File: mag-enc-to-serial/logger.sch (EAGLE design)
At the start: 28 parts, among them IC1 75176AD, IC2 REG1117, U1 MSP430G2352IPW14

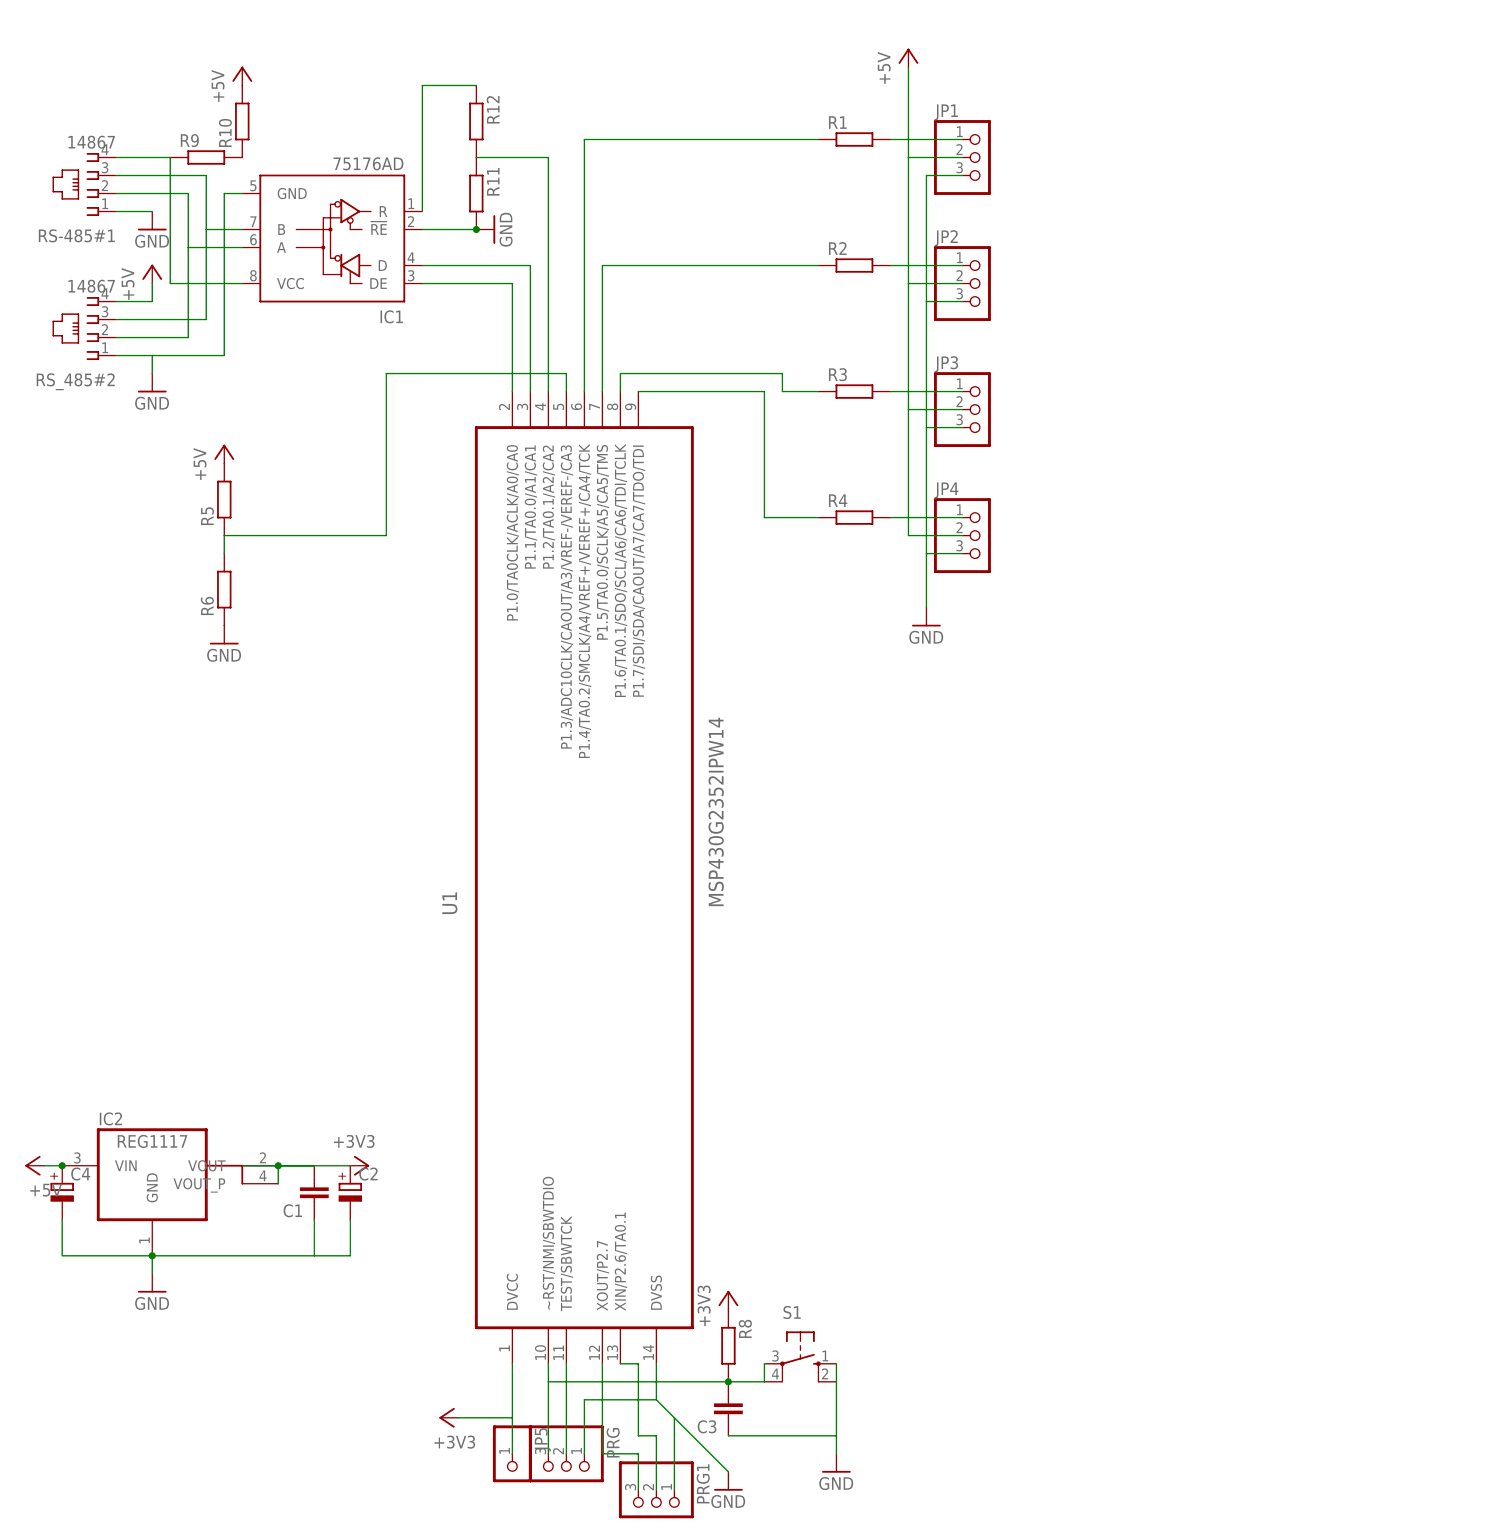
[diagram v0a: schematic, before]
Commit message: Magnetic encode with MSP430 board
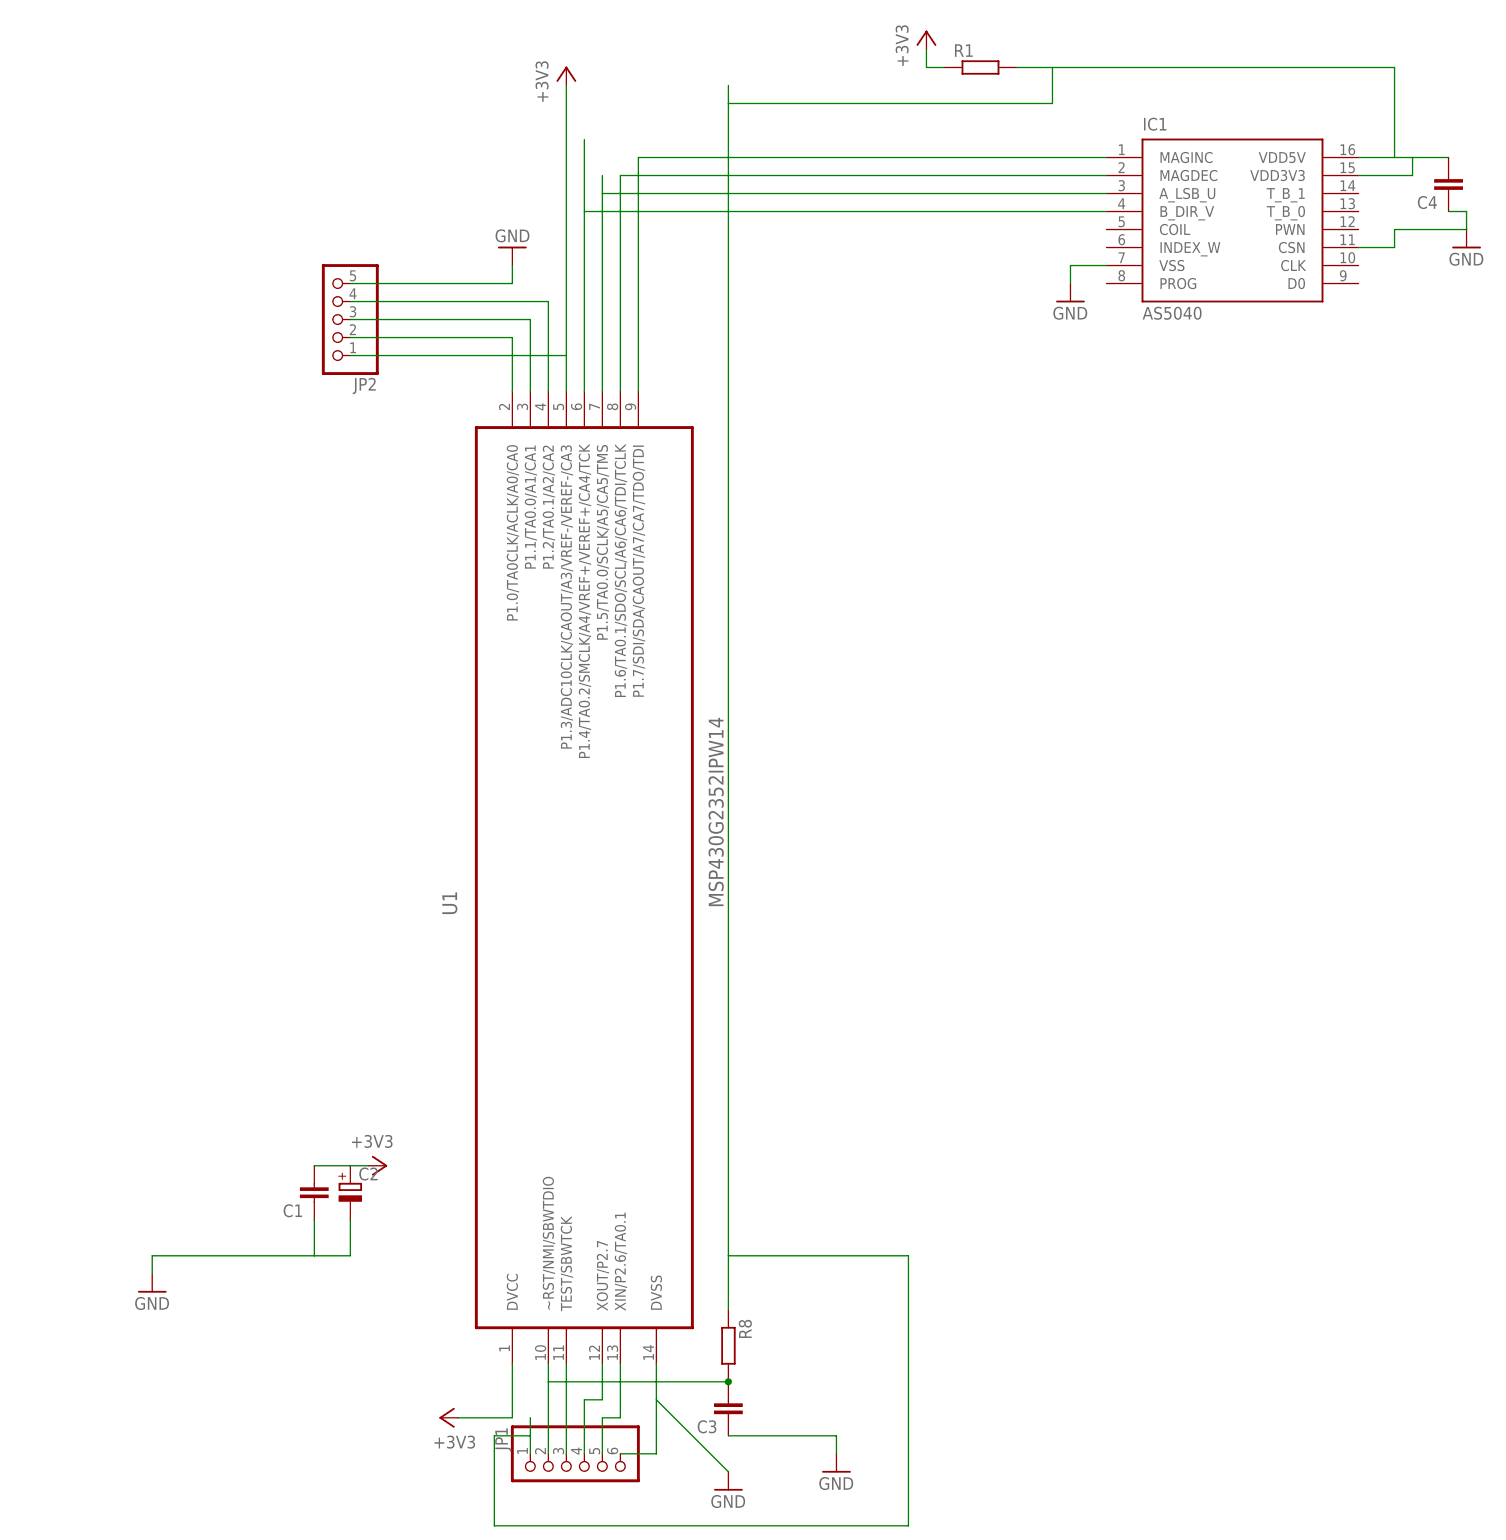
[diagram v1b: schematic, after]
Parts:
- removed IC2: REG1117, burr-brown:REG1117
- removed JP3, JP4, PRG, PRG1: (no value), pinhead:PINHD-1X3
- removed JP5: (no value), pinhead:PINHD-1X1
- removed R10, R9: (no value), rcl:R-EU_R1206
- removed R11, R12, R2, R3, R4, R5, R6: (no value), rcl:R-EU_R0805
- removed RS-485#1, RS_485#2: 14867, con-4ucon:14867
- removed S1: (no value), switch-omron:10-XX
- C4: device rcl:CPOL-EUE2,5-6E -> rcl:C-EUC0805
- IC1: value 75176AD -> AS5040; device 751xx:75176AD -> austriamicrosystems:AS5040
- JP1: device pinhead:PINHD-1X3 -> pinhead:PINHD-1X6/90
- JP2: device pinhead:PINHD-1X3 -> pinhead:PINHD-1X5/90
- R1: device rcl:R-EU_R0805 -> rcl:R-EU_R1206
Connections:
- removed net +5V: C4.+, IC2.VIN, JP1.2, JP2.2, JP3.2, JP4.2, R10.2, R5.2, RS_485#2.4
- removed net N$12: PRG1.2, U1.XIN/P2.6/TA0.1
- removed net N$14: IC1.DE, U1.P1.0/TA0CLK/ACLK/A0/CA0
- removed net N$16: PRG.2, U1.TEST/SBWTCK
- removed net N$18: PRG1.3, U1.XOUT/P2.7
- removed net N$19: R10.1, R9.2
- removed net N$20: IC1.VCC, R9.1, RS-485#1.4
- removed net N$21: IC1.R, R12.1
- removed net N$22: R11.1, R12.2, U1.P1.2/TA0.1/A2/CA2
- removed net N$8: JP1.1, R1.2
- removed net N$9: R3.1, U1.P1.6/TA0.1/SDO/SCL/A6/CA6/TDI/TCLK
- new net N$17: JP2.4, U1.P1.2/TA0.1/A2/CA2
- net +3V3: now also JP2.1, R1.1, U1.P1.3/ADC10CLK/CAOUT/A3/VREF-/VEREF-/CA3; no longer IC2.VOUT, IC2.VOUT_P, JP5.1, R8.1
- net GND: now also C4.1, IC1.CSN, IC1.VSS, JP1.6, JP2.5; no longer C4.-, IC1.!RE, IC1.GND, IC2.GND, JP1.3, JP2.3, JP3.3, JP4.3, PRG.1, PRG1.1, R11.2, R6.1, RS-485#1.1, RS_485#2.1, S1.S, S1.S1
- net N$1: now also JP1.3, U1.TEST/SBWTCK; no longer IC1.A, RS-485#1.2, RS_485#2.2
- net N$10: now also IC1.MAGDEC, U1.P1.6/TA0.1/SDO/SCL/A6/CA6/TDI/TCLK; no longer R2.1, U1.P1.5/TA0.0/SCLK/A5/CA5/TMS
- net N$11: now also IC1.MAGINC, U1.P1.7/SDI/SDA/CAOUT/A7/CA7/TDO/TDI; no longer R1.1, U1.P1.4/TA0.2/SMCLK/A4/VREF+/VEREF+/CA4/TCK
- net N$13: now also JP2.2, U1.P1.0/TA0CLK/ACLK/A0/CA0; no longer IC1.D, U1.P1.1/TA0.0/A1/CA1
- net N$15: now also JP1.2; no longer PRG.3, S1.P, S1.P1
- net N$2: now also JP2.3, U1.P1.1/TA0.0/A1/CA1; no longer IC1.B, RS-485#1.3, RS_485#2.3
- net N$3: now also JP1.4, U1.XOUT/P2.7; no longer R5.1, R6.2, U1.P1.3/ADC10CLK/CAOUT/A3/VREF-/VEREF-/CA3
- net N$4: now also IC1.B_DIR_V, U1.P1.4/TA0.2/SMCLK/A4/VREF+/VEREF+/CA4/TCK; no longer R4.1, U1.P1.7/SDI/SDA/CAOUT/A7/CA7/TDO/TDI
- net N$5: now also IC1.A_LSB_U, U1.P1.5/TA0.0/SCLK/A5/CA5/TMS; no longer JP4.1, R4.2
- net N$6: now also C4.2, IC1.VDD3V3, IC1.VDD5V, JP1.1, R1.2, R8.1; no longer JP3.1, R3.2
- net N$7: now also JP1.5, U1.XIN/P2.6/TA0.1; no longer JP2.1, R2.2
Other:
- moved on the sheet: R1
